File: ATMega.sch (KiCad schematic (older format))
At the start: 32 parts, among them J9 Conn_02x03_Odd_Even, SW1 SW_Push, U1 ATmega2560-16AU, Y1 16MHz

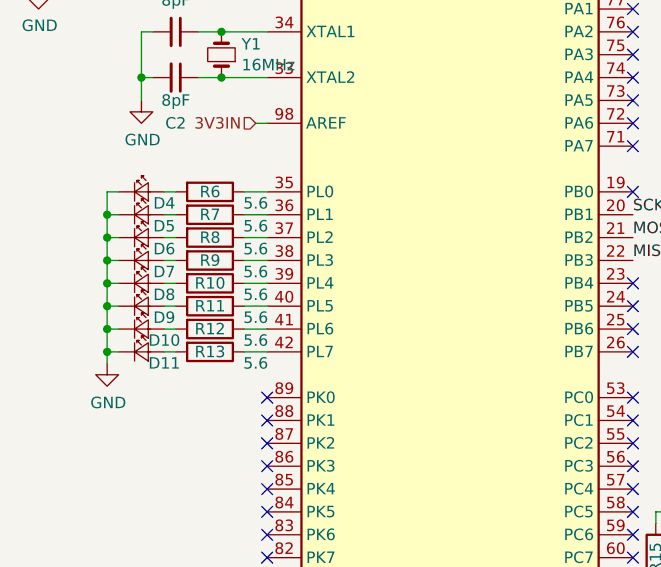
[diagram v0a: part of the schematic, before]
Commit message: fix debug LED resistors
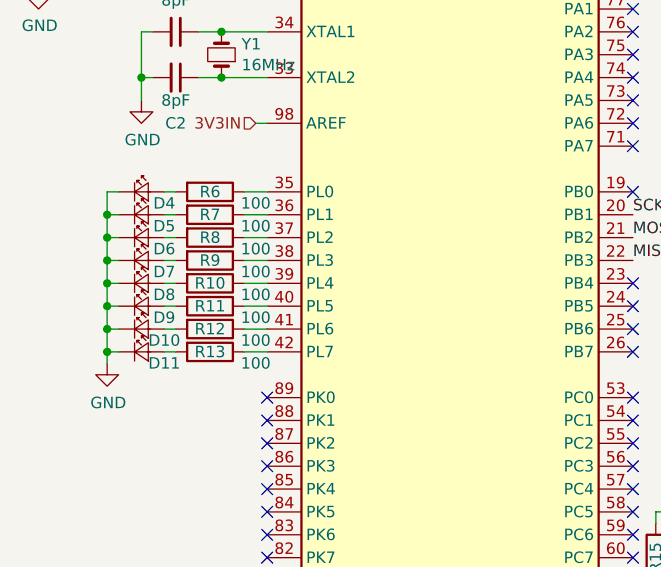
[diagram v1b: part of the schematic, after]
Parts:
- R10, R11, R12, R13, R6, R7, R8, R9: value 5.6 -> 100
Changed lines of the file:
@@
 P 2400 2250
 F 0 "R6" V 2400 2250 50  0000 C CNN
-F 1 "5.6" V 2450 2450 50  0000 C CNN
+F 1 "100" V 2450 2450 50  0000 C CNN
 F 2 "Resistor_SMD:R_0603_1608Metric" V 2330 2250 50  0001 C CNN
 F 3 "~" H 2400 2250 50  0001 C CNN
@@
 P 2400 2350
 F 0 "R7" V 2400 2350 50  0000 C CNN
-F 1 "5.6" V 2450 2550 50  0000 C CNN
+F 1 "100" V 2450 2550 50  0000 C CNN
 F 2 "Resistor_SMD:R_0603_1608Metric" V 2330 2350 50  0001 C CNN
 F 3 "~" H 2400 2350 50  0001 C CNN
@@
 P 2400 2450
 F 0 "R8" V 2400 2450 50  0000 C CNN
-F 1 "5.6" V 2450 2650 50  0000 C CNN
+F 1 "100" V 2450 2650 50  0000 C CNN
 F 2 "Resistor_SMD:R_0603_1608Metric" V 2330 2450 50  0001 C CNN
 F 3 "~" H 2400 2450 50  0001 C CNN
@@
 P 2400 2550
 F 0 "R9" V 2400 2550 50  0000 C CNN
-F 1 "5.6" V 2450 2750 50  0000 C CNN
+F 1 "100" V 2450 2750 50  0000 C CNN
 F 2 "Resistor_SMD:R_0603_1608Metric" V 2330 2550 50  0001 C CNN
 F 3 "~" H 2400 2550 50  0001 C CNN
@@
 P 2400 2650
 F 0 "R10" V 2400 2650 50  0000 C CNN
-F 1 "5.6" V 2450 2850 50  0000 C CNN
+F 1 "100" V 2450 2850 50  0000 C CNN
 F 2 "Resistor_SMD:R_0603_1608Metric" V 2330 2650 50  0001 C CNN
 F 3 "~" H 2400 2650 50  0001 C CNN
@@
 P 2400 2750
 F 0 "R11" V 2400 2750 50  0000 C CNN
-F 1 "5.6" V 2450 2950 50  0000 C CNN
+F 1 "100" V 2450 2950 50  0000 C CNN
 F 2 "Resistor_SMD:R_0603_1608Metric" V 2330 2750 50  0001 C CNN
 F 3 "~" H 2400 2750 50  0001 C CNN
@@
 P 2400 2850
 F 0 "R12" V 2400 2850 50  0000 C CNN
-F 1 "5.6" V 2450 3050 50  0000 C CNN
+F 1 "100" V 2450 3050 50  0000 C CNN
 F 2 "Resistor_SMD:R_0603_1608Metric" V 2330 2850 50  0001 C CNN
 F 3 "~" H 2400 2850 50  0001 C CNN
@@
 P 2400 2950
 F 0 "R13" V 2400 2950 50  0000 C CNN
-F 1 "5.6" V 2450 3150 50  0000 C CNN
+F 1 "100" V 2450 3150 50  0000 C CNN
 F 2 "Resistor_SMD:R_0603_1608Metric" V 2330 2950 50  0001 C CNN
 F 3 "~" H 2400 2950 50  0001 C CNN
